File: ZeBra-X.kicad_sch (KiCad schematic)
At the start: 0 parts

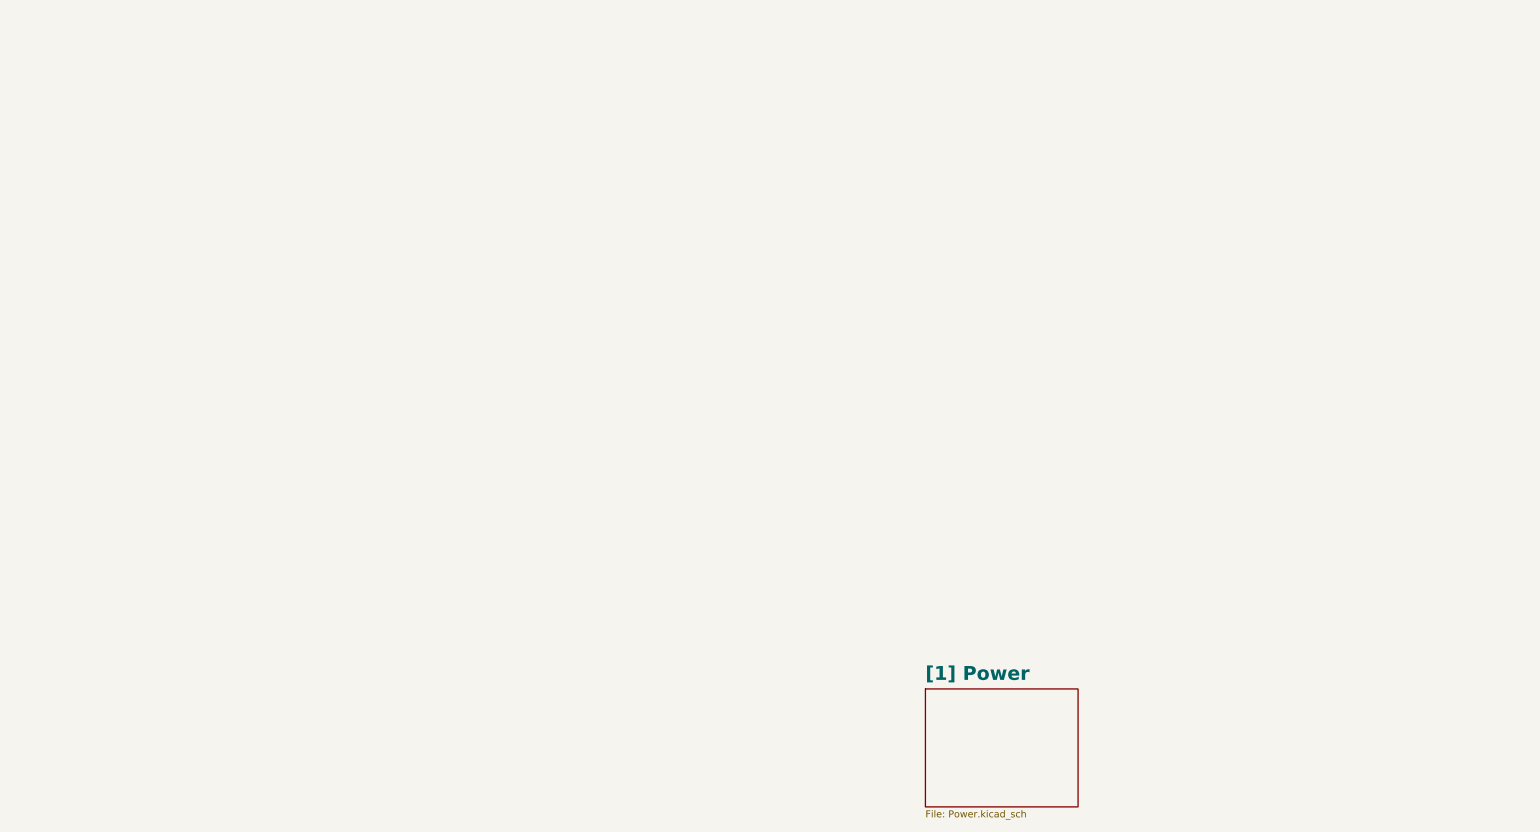
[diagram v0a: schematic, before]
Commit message: Schematic page 2 done, Zynq Power
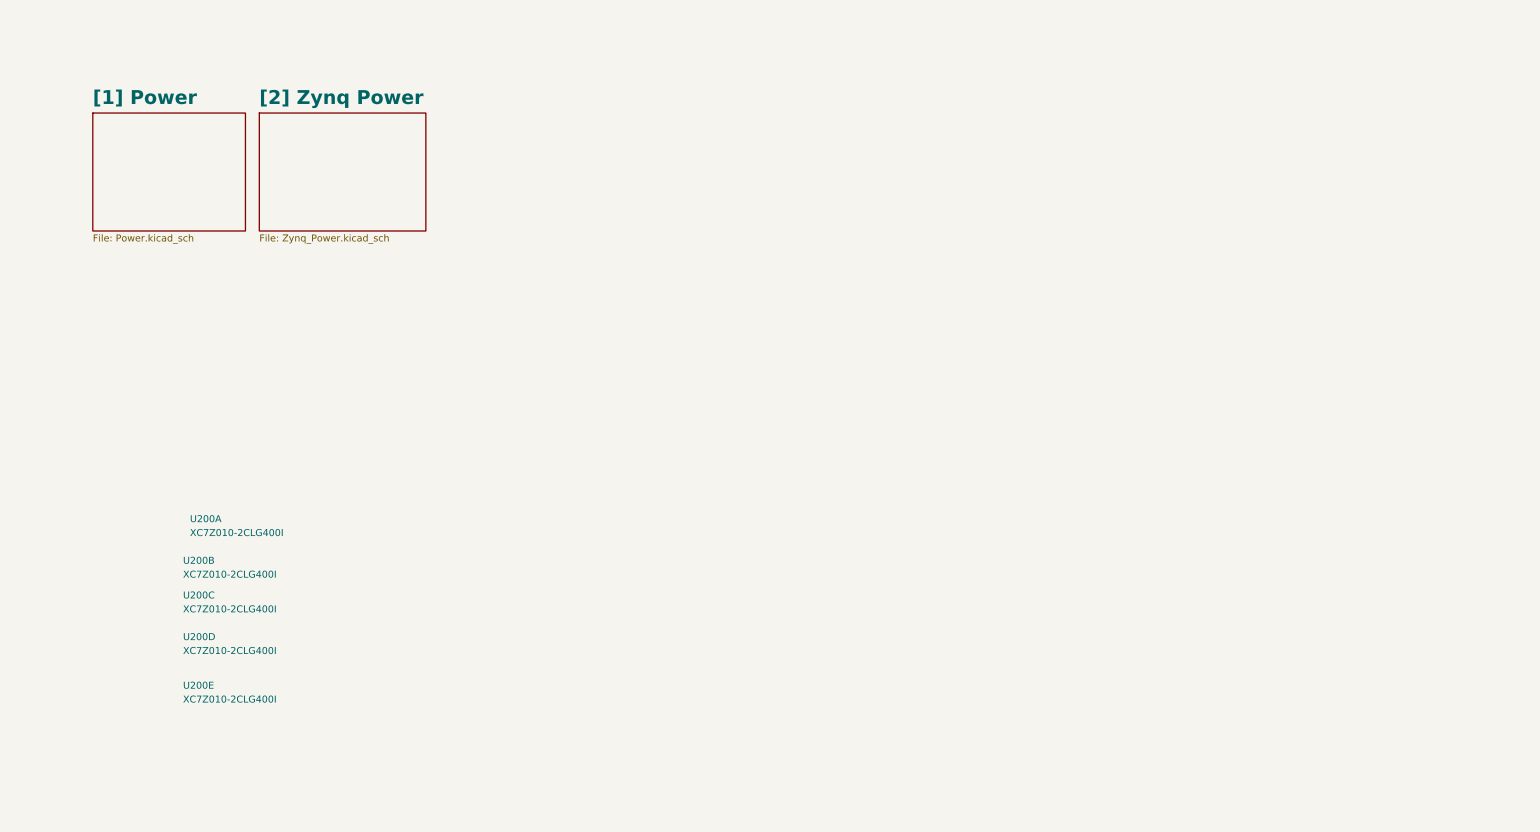
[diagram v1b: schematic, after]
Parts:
- added U200: XC7Z010-2CLG400I, ZeBra_footprints:CLG400_XIL, symbol ZeBra-X:XC7Z010-2CLG400I
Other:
- added sheet [2] Zynq Power (Zynq_Power.kicad_sch)
- title: ZeBra-X: A Xylinx Zynq Demo Board -> ZeBra-X: A Xilinx Zynq Demo Board

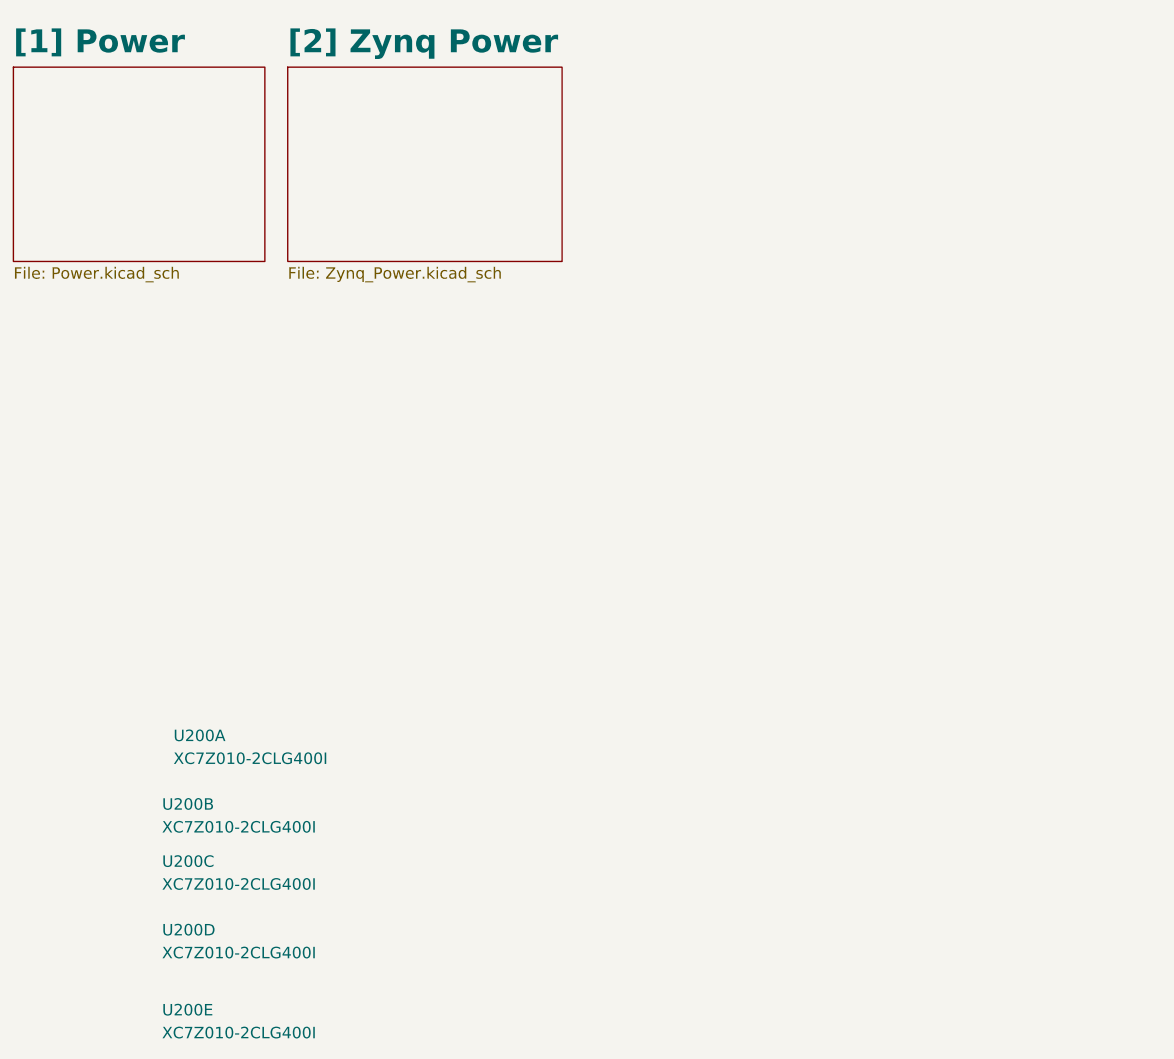
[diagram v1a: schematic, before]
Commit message: Finished page 3 of schematic: Zynq Config, JTAG, Debug
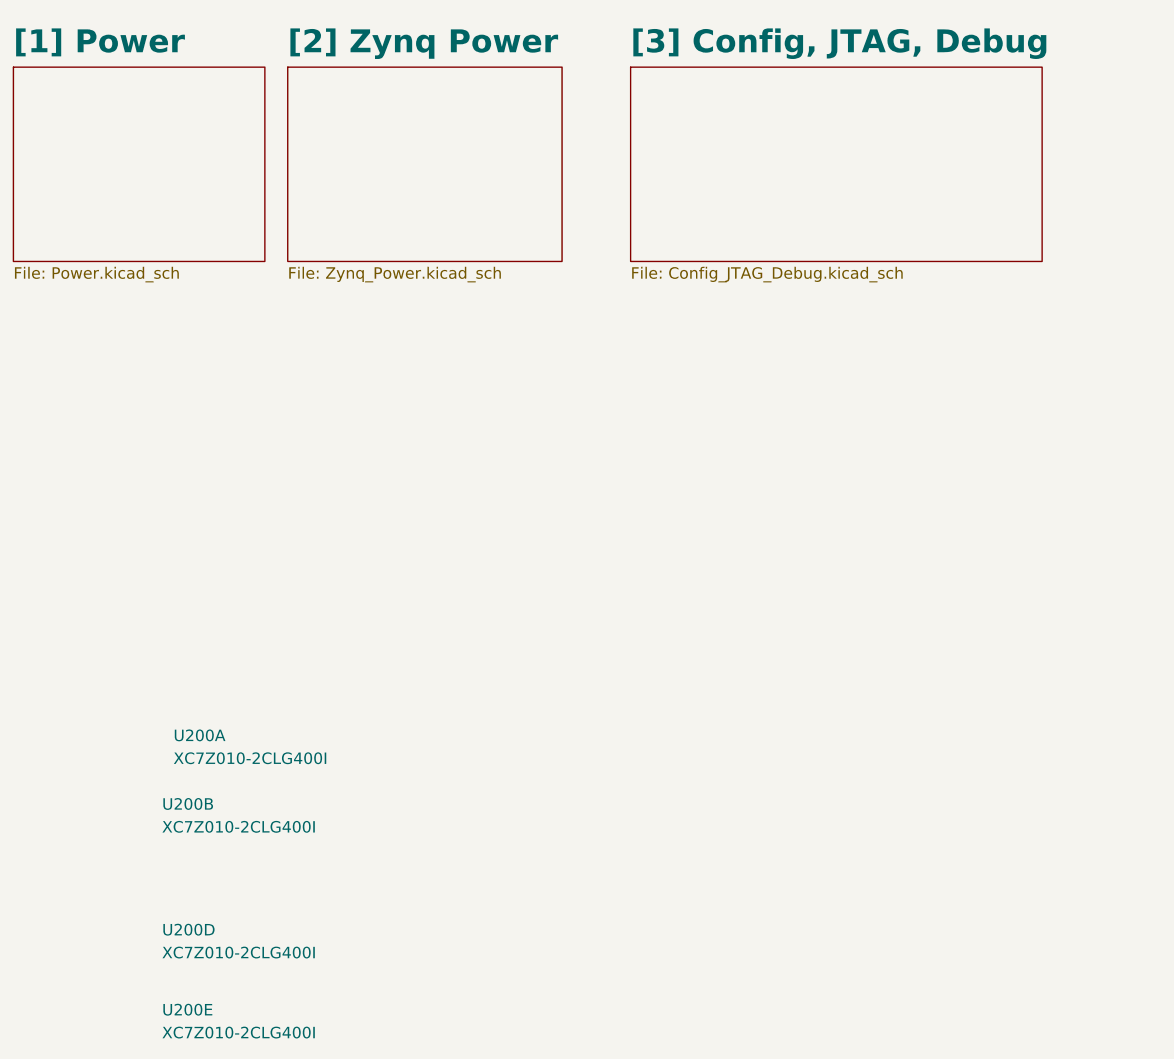
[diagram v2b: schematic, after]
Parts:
- removed unit 3 of U200
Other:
- added sheet [3] Config, JTAG, Debug (Config_JTAG_Debug.kicad_sch)

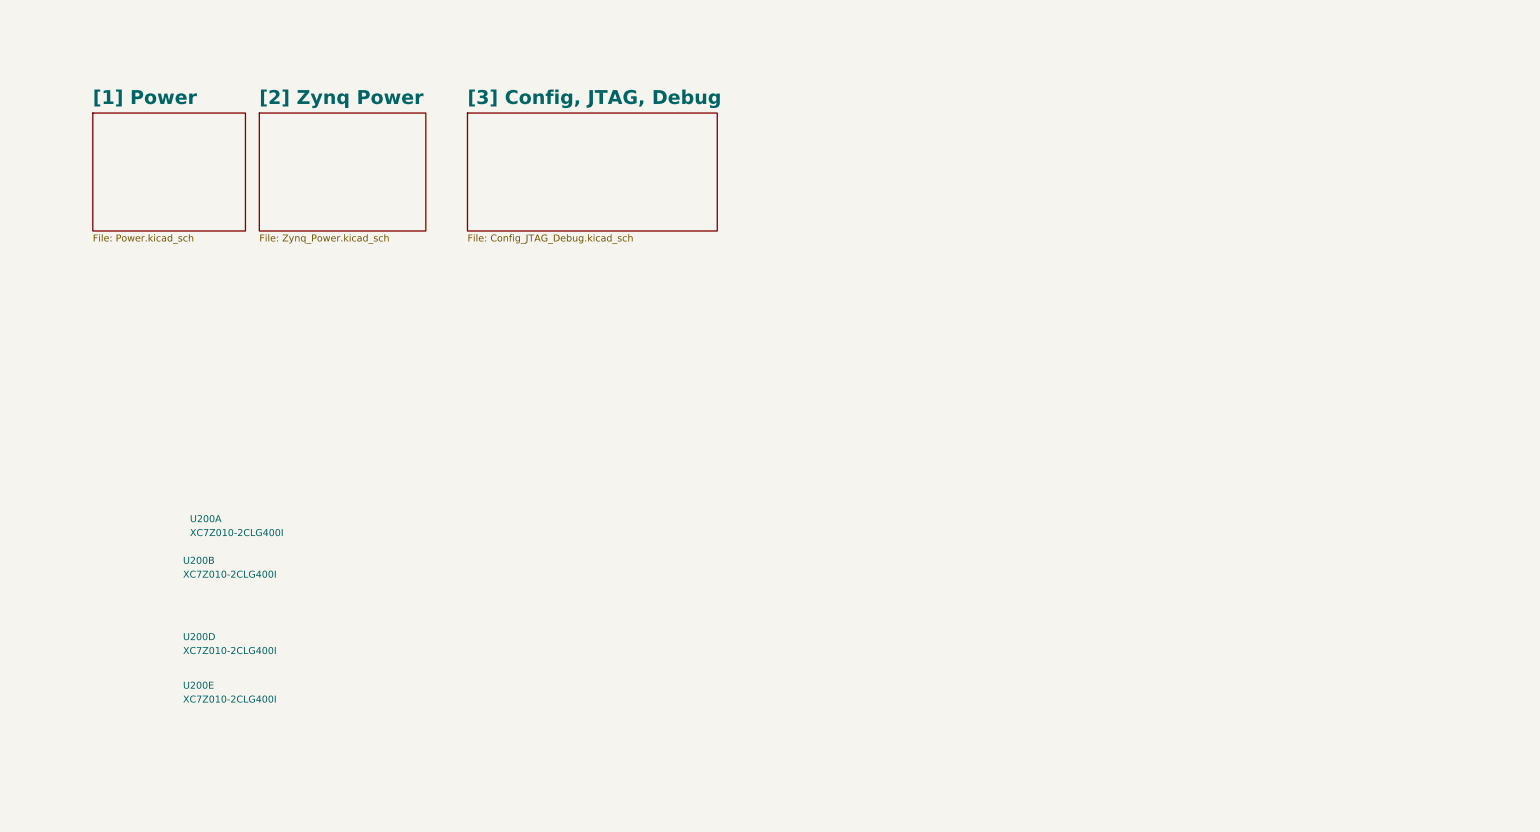
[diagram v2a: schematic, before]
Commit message: Finished schematic page 4: Zynq Processing System (PS), includes 128MBit QSPI flash, 33.33 MHz PS Clock, and 4Gbyte EMMC Memory
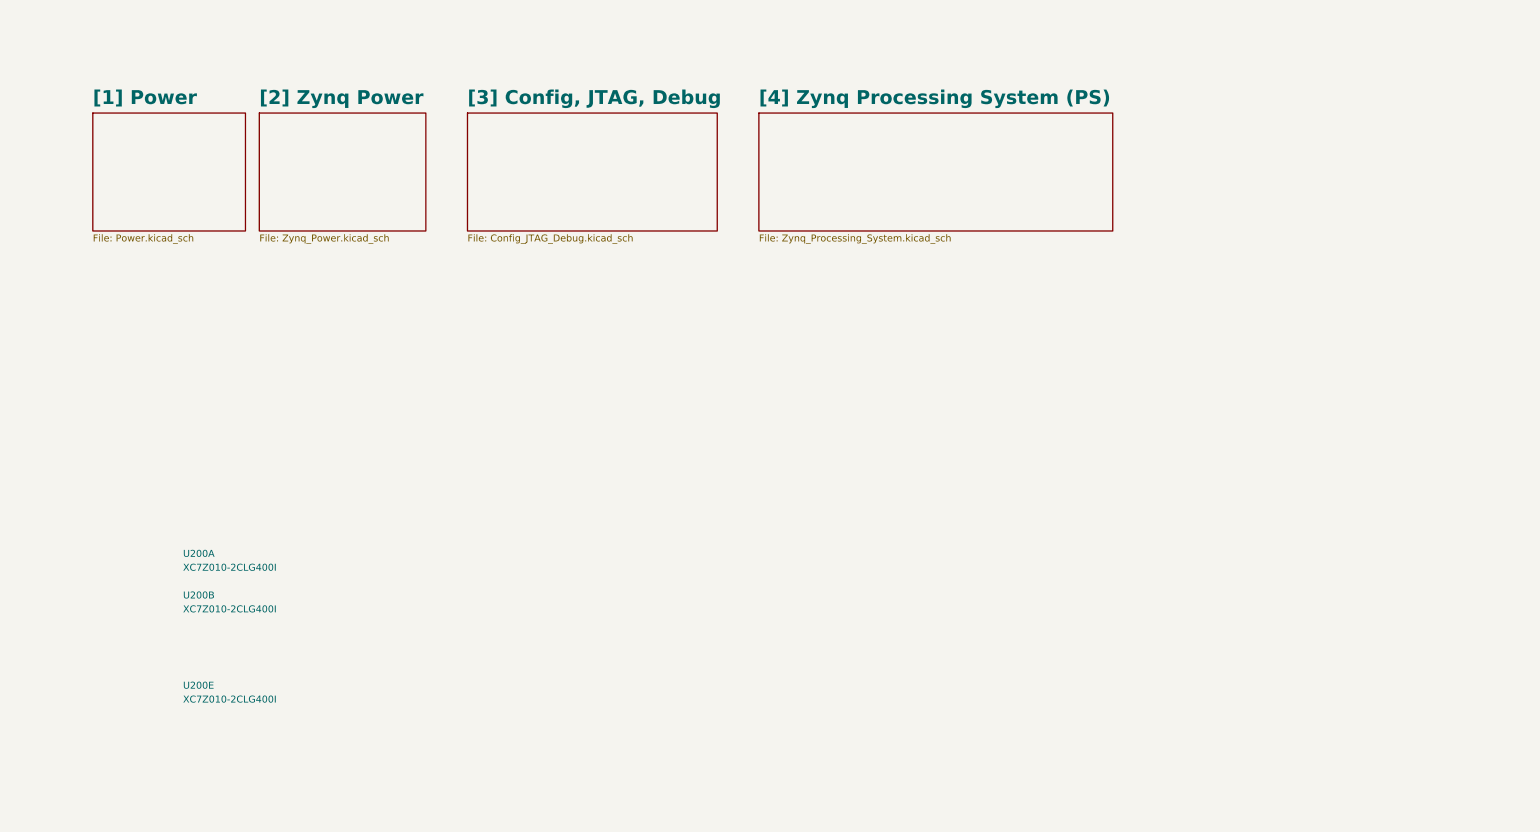
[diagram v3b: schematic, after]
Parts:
- removed unit 4 of U200
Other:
- added sheet [4] Zynq Processing System (PS) (Zynq_Processing_System.kicad_sch)

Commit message: Added shematic sheet 5:Zynq Programmable Logic (PL)
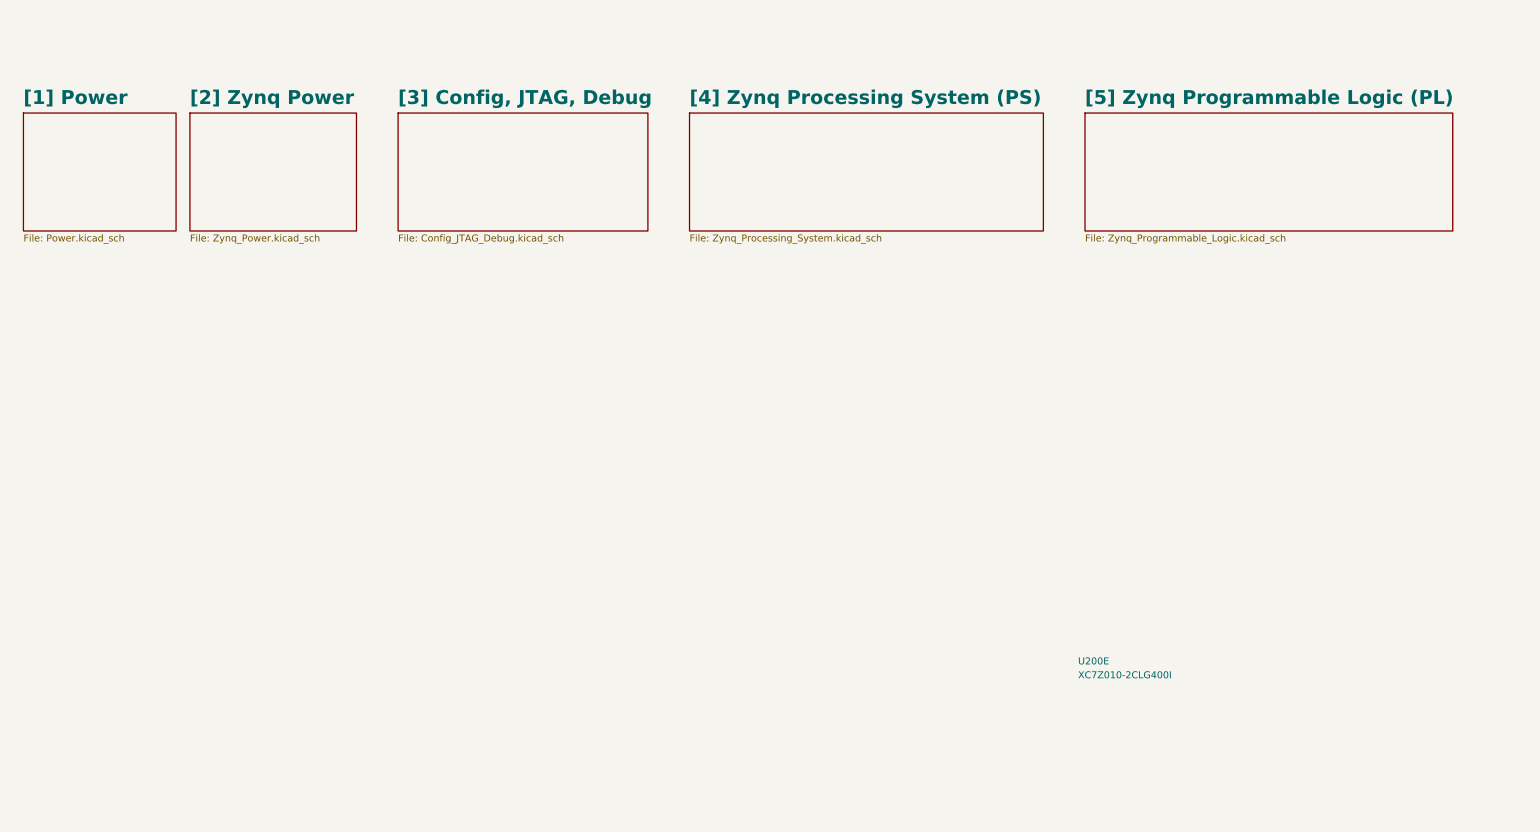
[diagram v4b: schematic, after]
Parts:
- removed unit 1 of U200
- removed unit 2 of U200
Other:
- added sheet [5] Zynq Programmable Logic (PL) (Zynq_Programmable_Logic.kicad_sch)

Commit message: Finished schematic page 6:Zynq DDR Interface & Termination
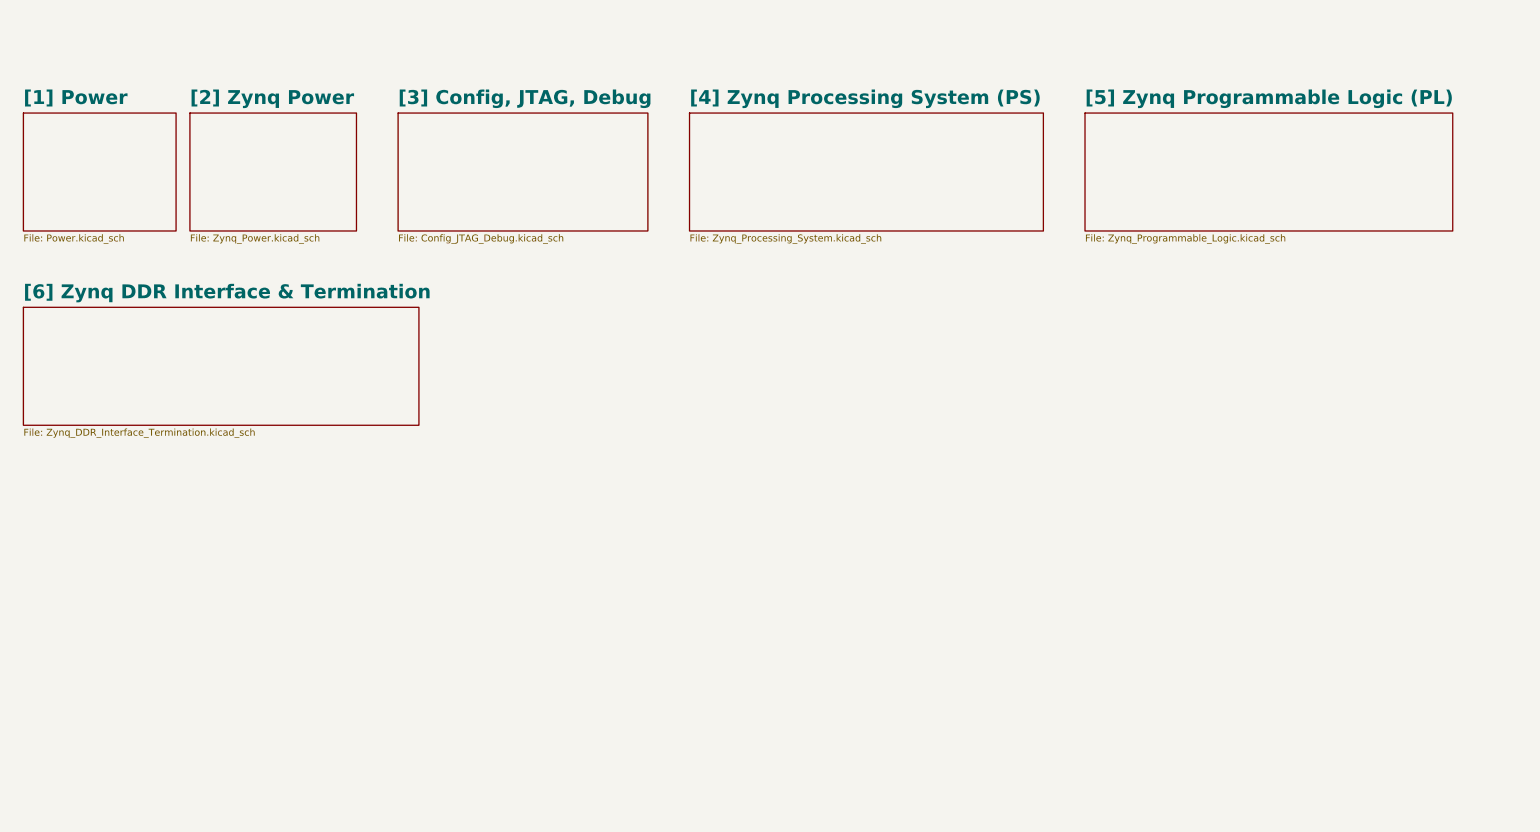
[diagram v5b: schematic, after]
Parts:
- removed U200: XC7Z010-2CLG400I, ZeBra_footprints:CLG400_XIL, symbol ZeBra-X:XC7Z010-2CLG400I
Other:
- added sheet [6] Zynq DDR Interface & Termination (Zynq_DDR_Interface_Termination.kicad_sch)
